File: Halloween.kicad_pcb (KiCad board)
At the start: 2 copper layers, 38.1 x 70.5 mm, 18 parts, among them SW1 SW_SPDT

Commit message: Changed board name to font, updated logo and LED direction
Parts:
- added G***: LOGO, Alpenglow:Alpenglow_Logo_Horiz_8mm, B.Cu at (133.9, 54.7)
- added G***: LOGO, Halloween:SPC board name 20x2.9mm, B.Cu at (167.3, 63.9)
- added G***: LOGO, Alpenglow:Alpenglow_Logo_Horiz_5mm, B.Cu at (167.4, 56.8)
- moved G*** 42.8 mm to (131.1, 37.5)
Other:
- net class Default removed
- board text added: "+ = LONG - = SHORT"
- board text removed: "LEDS: + = LONG - = SHORT"

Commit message: used oswald font for @alpenglowind
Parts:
- removed the G*** at (131.1, 37.5)
- removed the G*** at (133.9, 54.7)
- added G***: LOGO, Alpenglow:@AlpenglowIndOswald20mm, B.Cu at (166.5, 62.1)
- moved G*** 1.67 mm to (167.1, 55.1)
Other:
- board text removed: "@alpenglowind"
- board text removed: "ALPENGHOUL INDUSTRIES"

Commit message: updated LED long/short
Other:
- board text added: "+ LONG - SHORT"
- board text removed: "+ = LONG - = SHORT"
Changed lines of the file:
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@@
     (effects (font (size 1 1) (thickness 0.15)) (justify mirror))
   )
-  (gr_text "+ = LONG\n- = SHORT" (at 171.069 107.696) (layer "B.SilkS")
+  (gr_text "+ LONG\n- SHORT" (at 170.307 107.95) (layer "B.SilkS")
     (effects (font (size 1 1) (thickness 0.15)) (justify left mirror))
   )

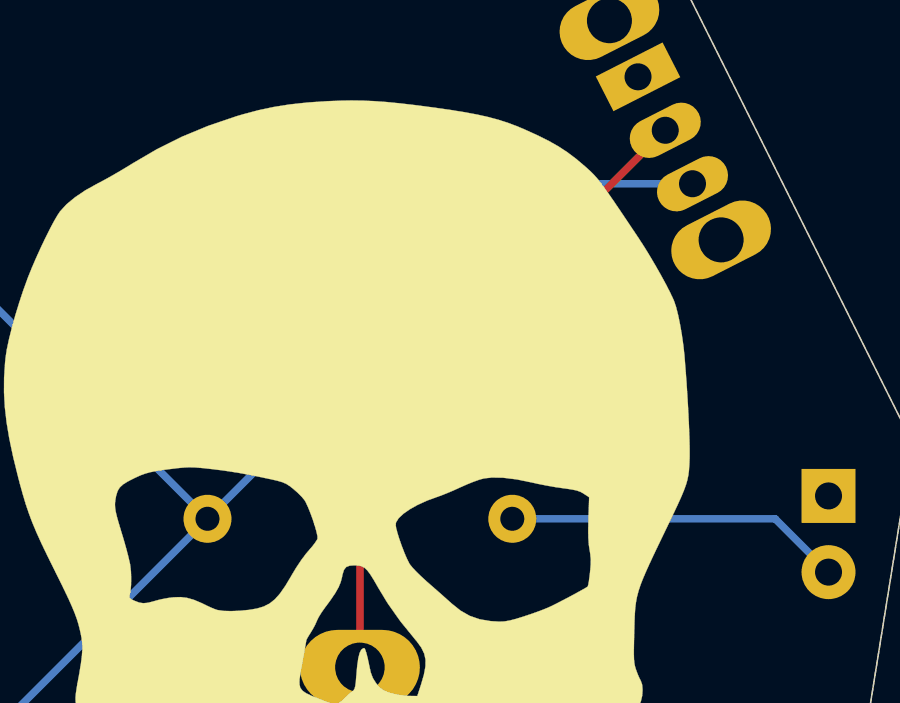
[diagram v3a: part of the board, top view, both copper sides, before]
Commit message: Updated switch footprint
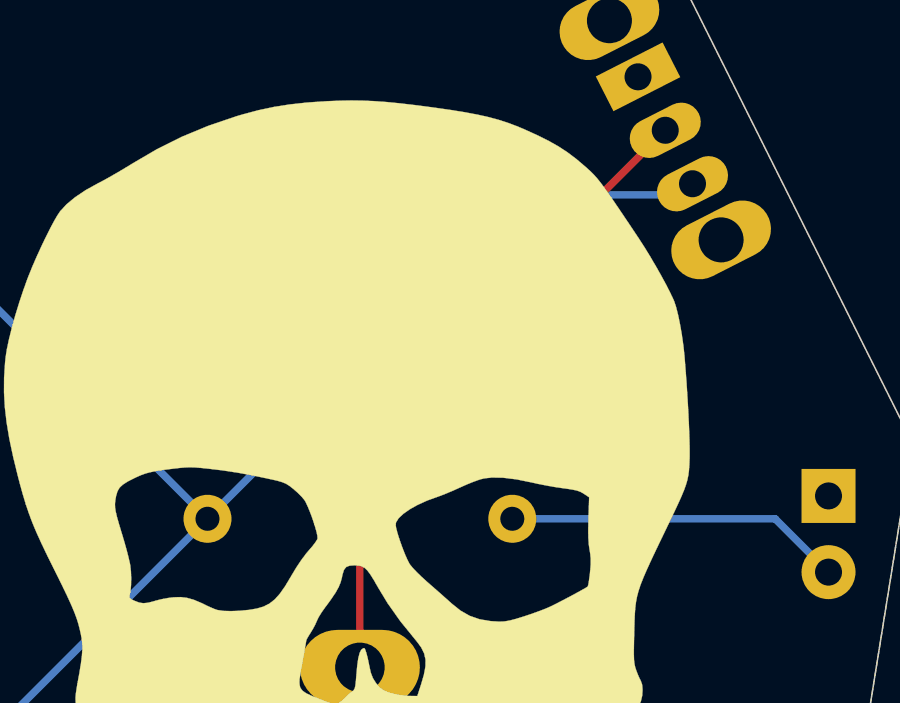
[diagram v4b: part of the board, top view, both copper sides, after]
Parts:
- SW1: footprint Alpenglow:SW_SLIDE_RTA -> Alpenglow:SW_SPDT_SLIDE_THRU_RTA
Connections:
- SW1 pad 1: Net-(SW1-Pad1) -> unconnected-(SW1-Pad1)
